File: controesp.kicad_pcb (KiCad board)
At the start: 2 copper layers, 216.9 x 86.5 mm, 73 parts, among them J1 Screw_Terminal_01x08, J13 Conn_01x19_Socket, J14 Conn_01x16_Socket, J15 Screw_Terminal_01x02, J16 Conn_01x19_Socket, J17 Conn_01x19_Socket, J2 Screw_Terminal_01x04, J3 Conn_01x14_Socket, J4 Conn_01x14_Pin, J5 Conn_01x16_Pin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

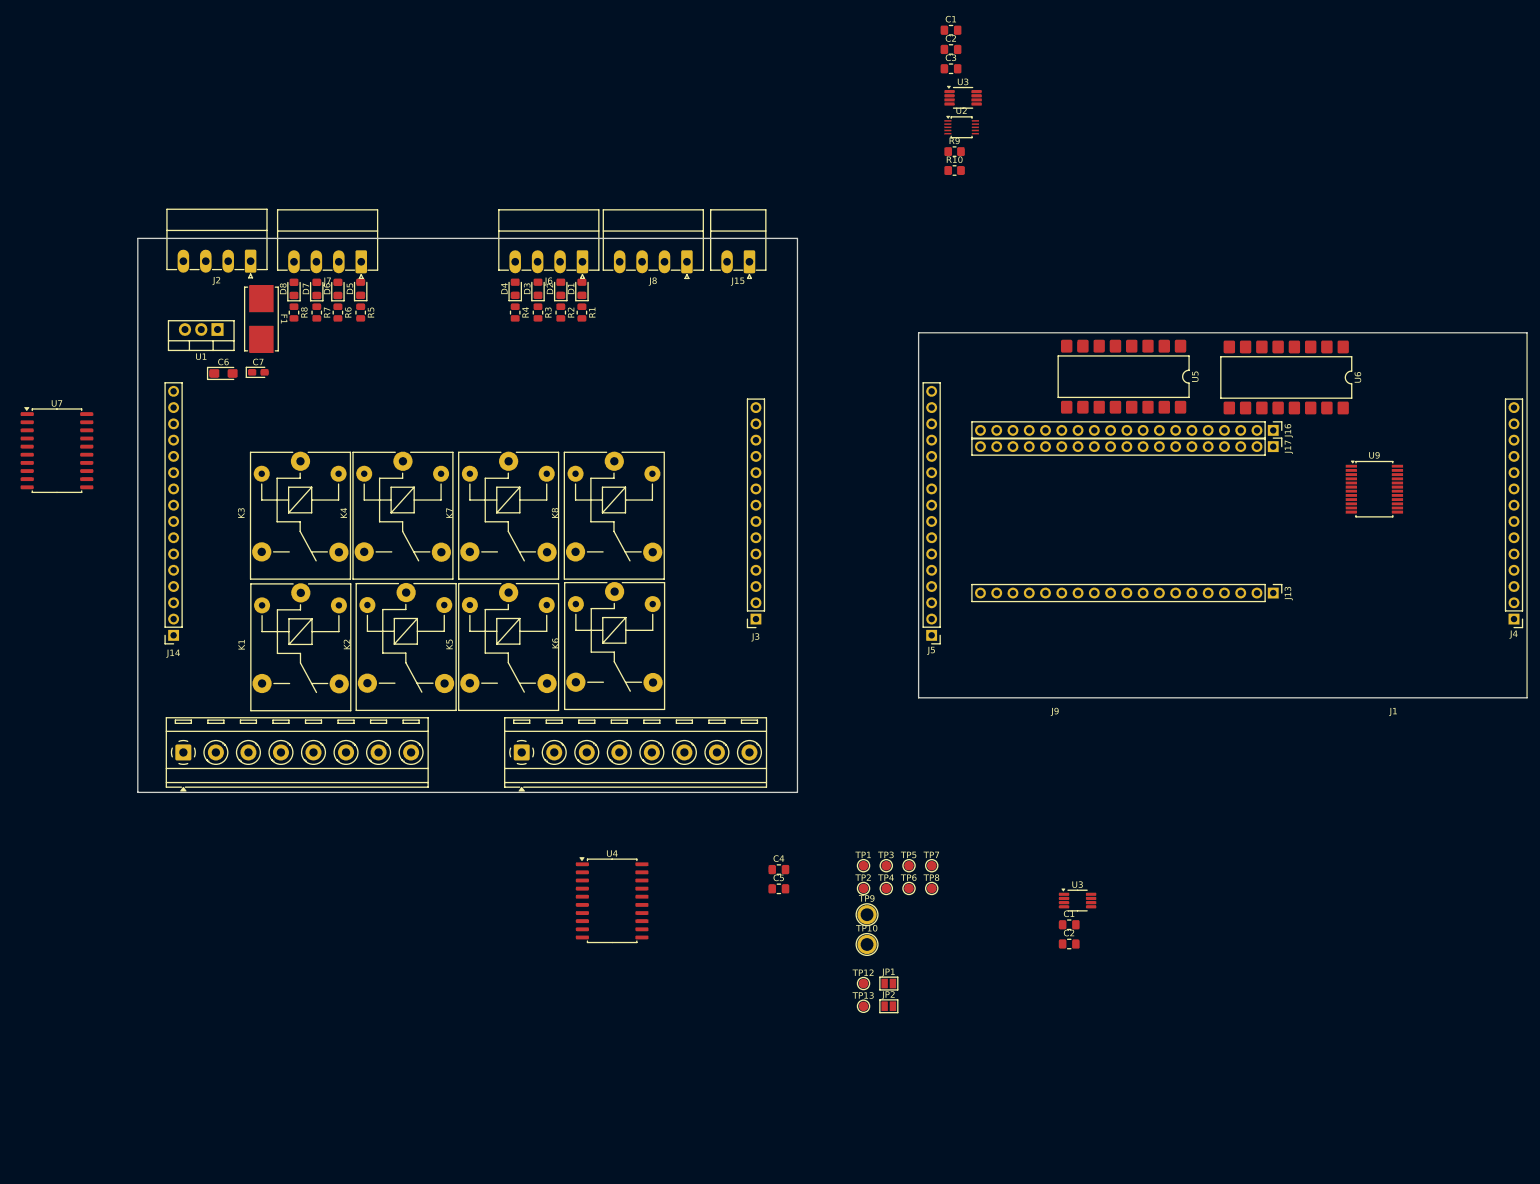
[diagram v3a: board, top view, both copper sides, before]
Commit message: hat routing finished
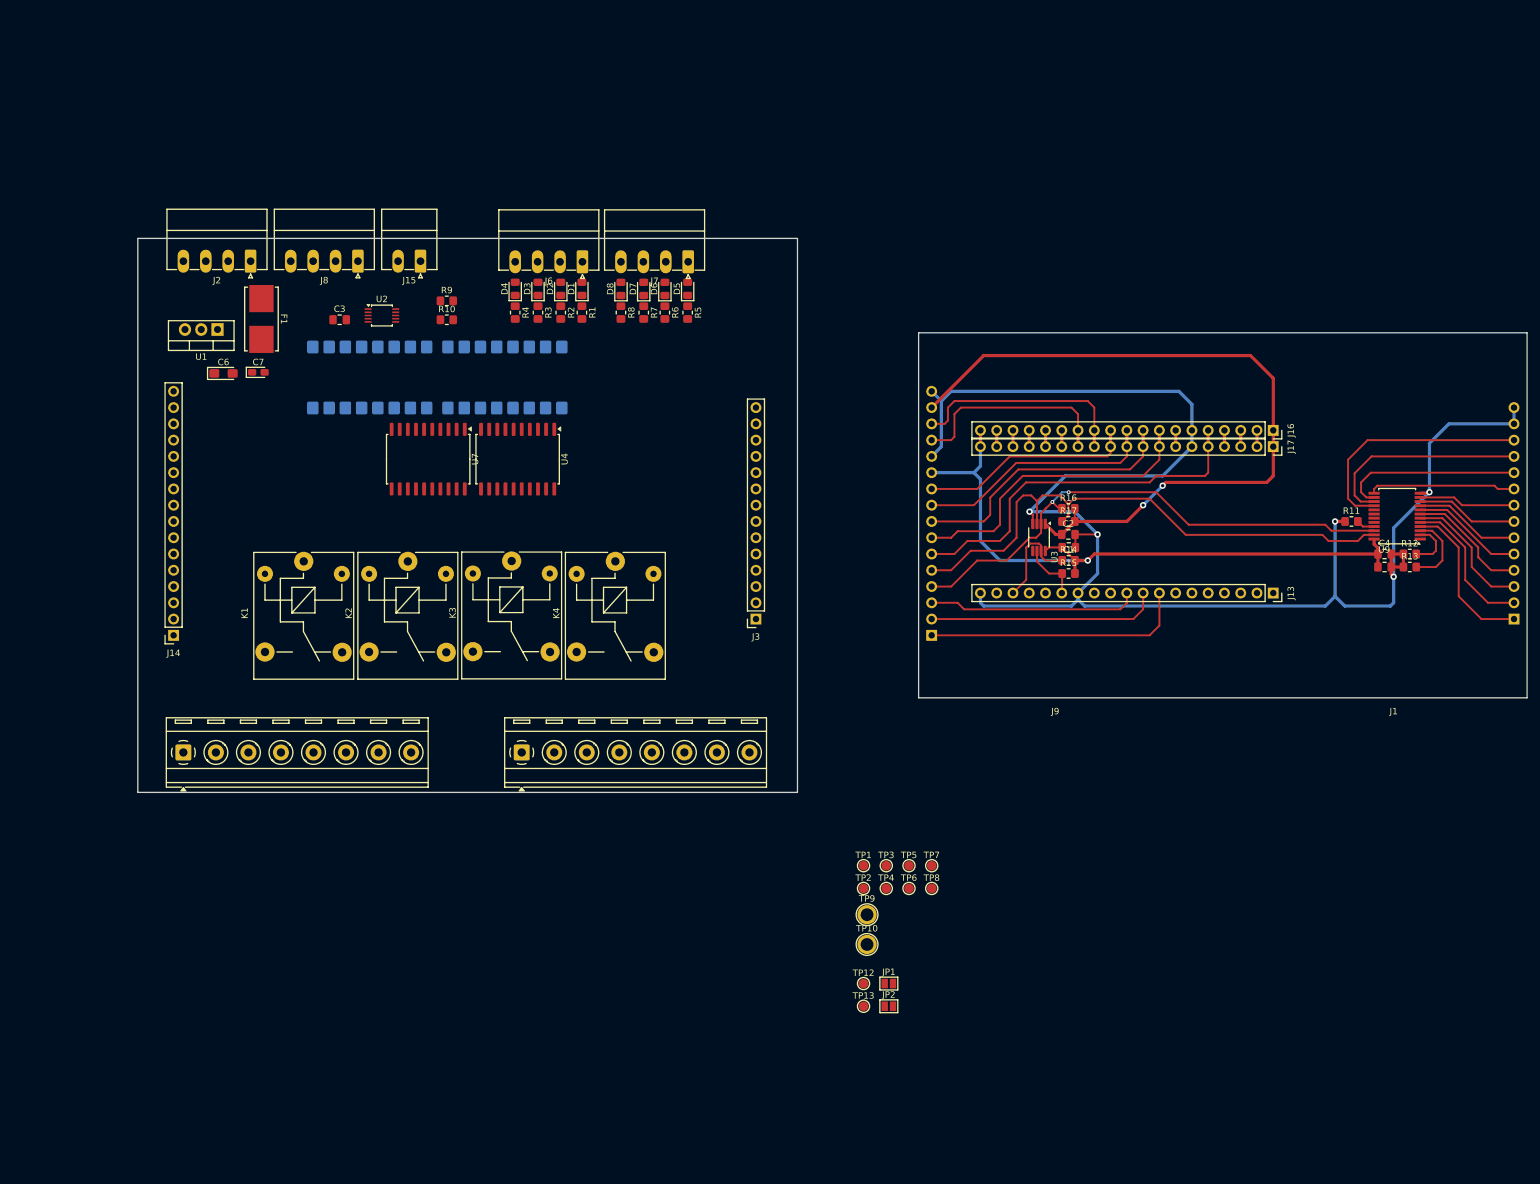
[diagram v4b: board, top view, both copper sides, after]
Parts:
- removed the C1 at (176.8, 17.3)
- removed the C1 at (195.2, 157.0)
- removed the C2 at (176.8, 20.3)
- removed the C2 at (195.2, 160.0)
- removed K5, K6, K7, K8: SANYOU_SRD-S-124D, Relay_THT:Relay_SPDT_SANYOU_SRD_Series_Form_C
- removed the U3 at (196.5, 153.2)
- removed the U3 at (178.6, 27.8)
- added C1: 100nF, Capacitor_SMD:C_0805_2012Metric_Pad1.18x1.45mm_HandSolder, F.Cu at (195.1, 98.0)
- added C2: 100nF, Capacitor_SMD:C_0805_2012Metric_Pad1.18x1.45mm_HandSolder, F.Cu at (195.1, 96.0)
- added R11: 0, Resistor_SMD:R_0805_2012Metric_Pad1.20x1.40mm_HandSolder, F.Cu at (239.3, 94.0)
- added R12: 0, Resistor_SMD:R_0805_2012Metric_Pad1.20x1.40mm_HandSolder, F.Cu at (248.4, 99.1)
- added R13: 0, Resistor_SMD:R_0805_2012Metric_Pad1.20x1.40mm_HandSolder, F.Cu at (248.4, 101.1)
- added R14: 10k, Resistor_SMD:R_0805_2012Metric_Pad1.20x1.40mm_HandSolder, F.Cu at (195.1, 100.1)
- added R15: 10k, Resistor_SMD:R_0805_2012Metric_Pad1.20x1.40mm_HandSolder, F.Cu at (195.1, 102.1)
- added R16: 10k, Resistor_SMD:R_0805_2012Metric_Pad1.20x1.40mm_HandSolder, F.Cu at (195.1, 91.9)
- added R17: 10k, Resistor_SMD:R_0805_2012Metric_Pad1.20x1.40mm_HandSolder, F.Cu at (195.1, 94.0)
- added U3: TCA9517ADGK, Package_SO:VSSOP-8_3x3mm_P0.65mm, F.Cu at (190.5, 96.5)
- J13, J16, J17: footprint Connector_PinHeader_2.54mm:PinHeader_1x19_P2.54mm_Vertical -> Connector_PinSocket_2.54mm:PinSocket_1x19_P2.54mm_Vertical
- J4, J5, U5, U6: moved to B.Cu
- R1, R2, R3, R4, R5, R6, R7, R8: footprint Resistor_SMD:R_0805_2012Metric -> Resistor_SMD:R_0805_2012Metric_Pad1.20x1.40mm_HandSolder
- moved U6 143.1 mm to (86.0, 71.5)
- moved C5 107.1 mm to (244.5, 101.1)
- moved C4 106.6 mm to (244.5, 99.1)
- moved C3 103.2 mm to (81.3, 62.5)
- moved U5 96.6 mm to (107.1, 71.5)
- moved U2 95.2 mm to (87.9, 61.8)
- moved R10 82.6 mm to (98.0, 62.5)
- moved R9 82.6 mm to (98.0, 59.5)
- moved U4 70.5 mm to (109.1, 84.2), turned to -90 degrees
- moved U7 58.0 mm to (95.1, 84.2), turned to -90 degrees
- moved J8 51.4 mm to (84.2, 53.3)
- moved J15 51.4 mm to (93.9, 53.3)
- moved D6 51.1 mm to (132.1, 57.7)
- moved R6 51.1 mm to (132.1, 61.4)
- moved D5 51.1 mm to (135.6, 57.6)
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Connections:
- J14 pad 1: /input/DI1 -> RX2
- J14 pad 10: TX2 -> /input/DI6
- J14 pad 11: RX2 -> +3V3
- J14 pad 13: /input/SCL -> /input/DI7
- J14 pad 14: /input/SDA -> /input/DI8
- J14 pad 2: /input/DI2 -> TX2
- J14 pad 3: /input/DI3 -> /input/SCL
- J14 pad 4: /input/DI4 -> /input/SDA
- J14 pad 5: /input/DI5 -> /input/DI1
- J14 pad 6: /input/DI6 -> /input/DI2
- J14 pad 7: /input/DI7 -> /input/DI3
- J14 pad 8: /input/DI8 -> /input/DI4
- J14 pad 9: +3V3 -> /input/DI5
- J4 pad 13: GND -> /controesp_hat/GND
- J4 pad 14: GND -> /controesp_hat/GND
- J5 pad 1: /controesp_hat/32 -> /controesp_hat/RX2
- J5 pad 10: /controesp_hat/TX2 -> /controesp_hat/25
- J5 pad 11: /controesp_hat/RX2 -> /controesp_hat/3V3
- J5 pad 12: unconnected-(J5-Pin_12-Pad12) -> /controesp_hat/GND
- J5 pad 13: /controesp_hat/SCL_5V -> /controesp_hat/32
- J5 pad 14: /controesp_hat/SDA_5V -> /controesp_hat/33
- J5 pad 2: /controesp_hat/33 -> /controesp_hat/TX2
- J5 pad 3: /controesp_hat/25 -> /controesp_hat/5
- J5 pad 4: /controesp_hat/26 -> /controesp_hat/SCL_5V
- J5 pad 5: /controesp_hat/27 -> /controesp_hat/SDA_5V
- J5 pad 6: /controesp_hat/14 -> /controesp_hat/13
- J5 pad 7: /controesp_hat/5 -> /controesp_hat/14
- J5 pad 8: /controesp_hat/13 -> /controesp_hat/27
- J5 pad 9: /controesp_hat/3V3 -> /controesp_hat/26
- J9 pad 1: COM2 -> GND
- U4 pad 11: Net-(U4-O8) -> Net-(J9-Pin_5)
- U4 pad 12: Net-(U4-O7) -> Net-(J9-Pin_4)
- U4 pad 13: Net-(U4-O6) -> Net-(J9-Pin_3)
- U4 pad 14: Net-(U4-O5) -> Net-(J9-Pin_2)
- U9 pad 2: /controesp_hat/GND -> Net-(U9-A1)
- U9 pad 21: /controesp_hat/GND -> Net-(U9-A0)
- U9 pad 3: /controesp_hat/GND -> Net-(U9-A2)
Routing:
- net /controesp_hat/GND: track 0.00 -> 256.6 mm, vias 0 -> 5
- net /controesp_hat/VCC: track 0.00 -> 115.5 mm, vias 0 -> 2
- net /controesp_hat/3V3: track 0.00 -> 102.8 mm, vias 0 -> 1
- net /controesp_hat/SDA_5V: track 0.00 -> 88.7 mm
- net /controesp_hat/SCL_5V: track 0.00 -> 81.4 mm, vias 0 -> 2
- net /controesp_hat/13: track 0.00 -> 58.0 mm
- net /controesp_hat/14: track 0.00 -> 47.6 mm
- net /controesp_hat/27: track 0.00 -> 42.9 mm
- net /controesp_hat/RX2: track 0.00 -> 41.3 mm
- net /controesp_hat/P13: track 0.00 -> 37.8 mm
- net /controesp_hat/26: track 0.00 -> 37.7 mm
- net /controesp_hat/TX2: track 0.00 -> 36.2 mm
- net /controesp_hat/33: track 0.00 -> 34.6 mm
- net /controesp_hat/25: track 0.00 -> 33.8 mm
- net /controesp_hat/P12: track 0.00 -> 32.9 mm
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
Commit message: started base layout
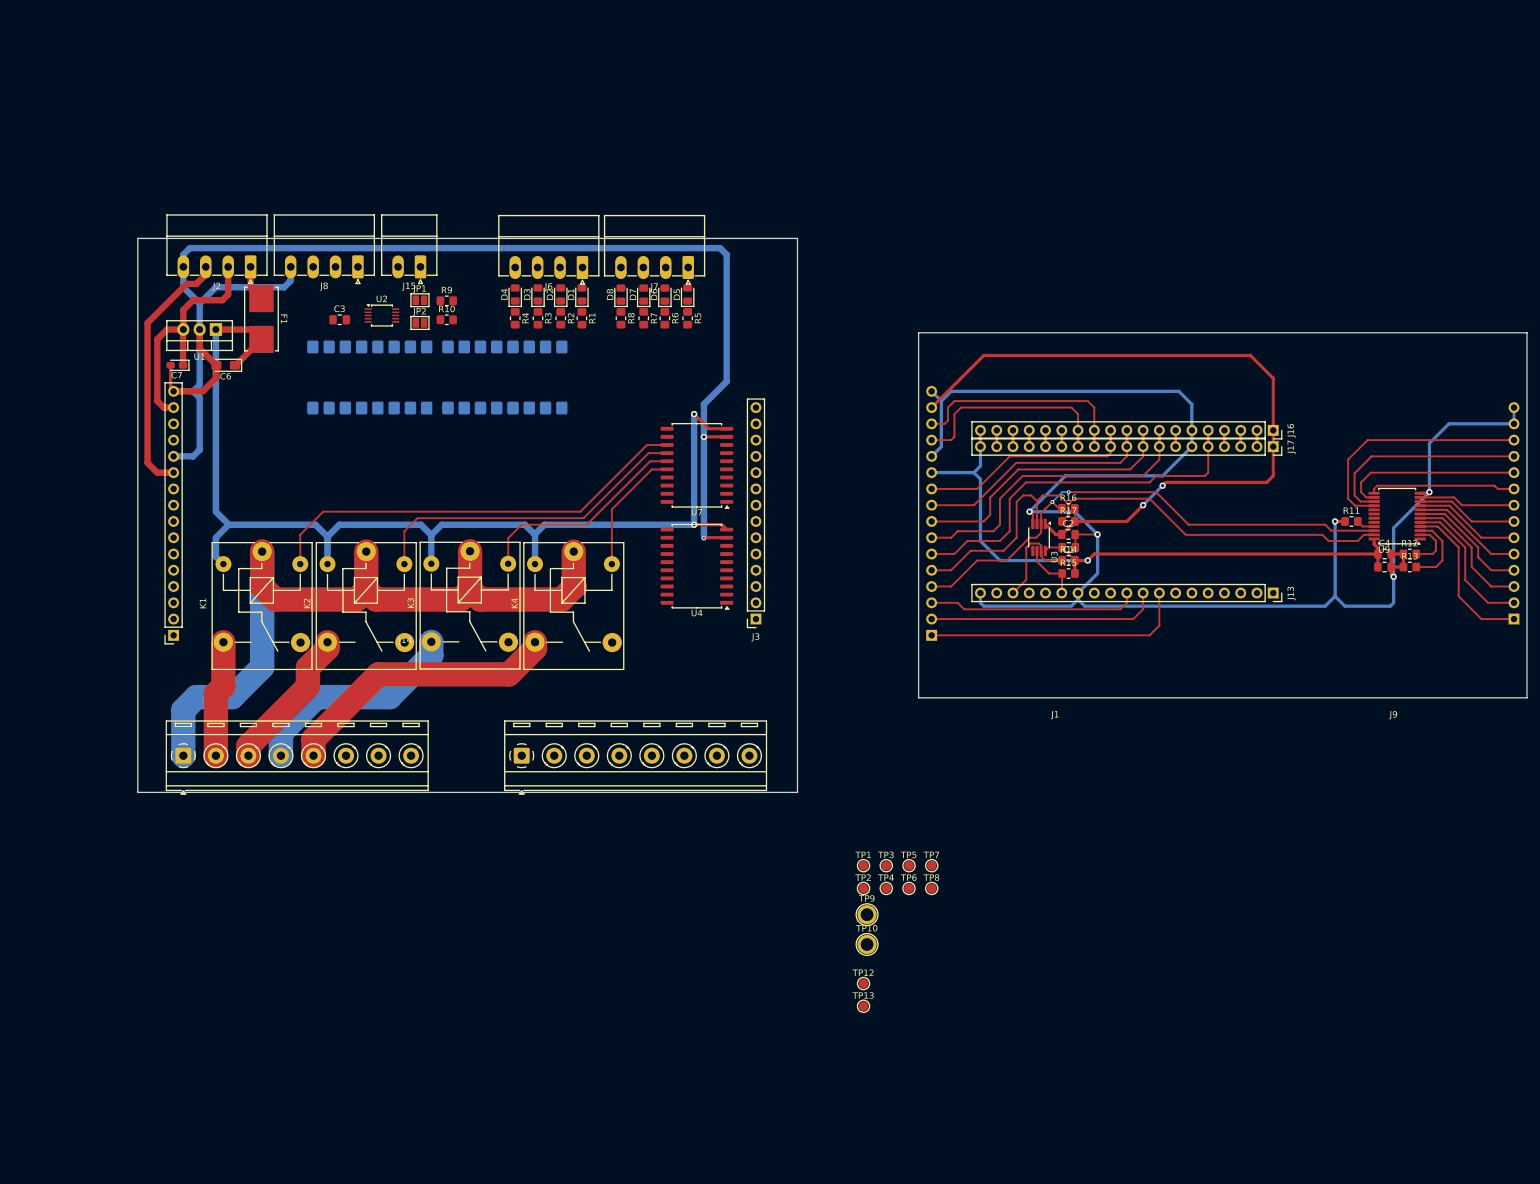
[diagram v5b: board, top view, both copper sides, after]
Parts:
- moved JP2 129.4 mm to (93.8, 63.0)
- moved JP1 129.4 mm to (93.8, 59.4)
- moved J1 52.8 mm to (56.9, 130.6)
- moved J9 52.8 mm to (109.7, 130.6)
- moved U7 42.0 mm to (137.1, 85.2), turned to 180 degrees
- moved U4 32.6 mm to (137.1, 101.0), turned to 180 degrees
- moved C7 12.8 mm to (55.9, 69.6), turned to 180 degrees
- moved K1 6.67 mm to (69.2, 98.7)
- moved K2 6.67 mm to (85.5, 98.7)
- moved K3 6.67 mm to (101.7, 98.6)
- moved K4 6.67 mm to (117.9, 98.7)
- moved C6 1.31 mm to (63.5, 69.6), turned to 180 degrees
- moved D1 0.89 mm to (119.1, 58.5)
- moved D2 0.89 mm to (115.8, 58.5)
- moved D3 0.89 mm to (112.3, 58.5)
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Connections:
- J3 pad 10: /powerOutput/DO10 -> DO10
- J3 pad 11: /powerOutput/DO11 -> DO11
- J3 pad 12: /powerOutput/DO12 -> DO12
- J3 pad 9: /powerOutput/DO9 -> DO9
- J9 pad 2: Net-(J9-Pin_2) -> unconnected-(J9-Pin_2-Pad2)
- J9 pad 3: Net-(J9-Pin_3) -> unconnected-(J9-Pin_3-Pad3)
- J9 pad 4: Net-(J9-Pin_4) -> unconnected-(J9-Pin_4-Pad4)
- J9 pad 5: Net-(J9-Pin_5) -> DO9
- K1 pad 5: Net-(U4-O1) -> DO14
- K2 pad 5: Net-(U4-O2) -> DO13
- K3 pad 5: Net-(U4-O3) -> DO12
- K4 pad 5: Net-(U4-O4) -> DO11
- TP1 pad 1: Net-(U4-O1) -> DO14
- TP2 pad 1: Net-(U4-O2) -> DO13
- TP3 pad 1: Net-(U4-O3) -> DO12
- TP4 pad 1: Net-(U4-O4) -> DO11
- U4 pad 11: Net-(J9-Pin_5) -> unconnected-(U4-O8-Pad11)
- U4 pad 12: Net-(J9-Pin_4) -> unconnected-(U4-O7-Pad12)
- U4 pad 13: Net-(J9-Pin_3) -> unconnected-(U4-O6-Pad13)
- U4 pad 14: Net-(J9-Pin_2) -> unconnected-(U4-O5-Pad14)
- U4 pad 15: Net-(U4-O4) -> unconnected-(U4-O4-Pad15)
- U4 pad 16: Net-(U4-O3) -> unconnected-(U4-O3-Pad16)
- U4 pad 17: Net-(U4-O2) -> unconnected-(U4-O2-Pad17)
- U4 pad 18: Net-(U4-O1) -> unconnected-(U4-O1-Pad18)
- U7 pad 1: /powerOutput/DO9 -> DO9
- U7 pad 13: DO6 -> DO14
- U7 pad 14: DO5 -> DO13
- U7 pad 15: DO4 -> DO12
- U7 pad 16: DO3 -> DO11
- U7 pad 17: DO2 -> DO10
- U7 pad 18: DO1 -> DO9
- U7 pad 2: /powerOutput/DO10 -> DO10
- U7 pad 3: /powerOutput/DO11 -> DO11
- U7 pad 4: /powerOutput/DO12 -> DO12
- U7 pad 5: unconnected-(U7-I5-Pad5) -> DO13
- U7 pad 6: unconnected-(U7-I6-Pad6) -> DO14
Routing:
- net GND: track 0.00 -> 216.7 mm, vias 0 -> 2
- net +24V: track 0.00 -> 171.3 mm, vias 0 -> 2
- net COM1: track 0.00 -> 116.2 mm
- net DO14: track 0.00 -> 67.7 mm
- net DO13: track 0.00 -> 51.2 mm
- net Net-(J1-Pin_5): track 0.00 -> 44.0 mm
- net +3V3: track 0.00 -> 40.0 mm
- net +5V: track 0.00 -> 38.3 mm
- net Net-(J1-Pin_4): track 0.00 -> 34.2 mm
- net DO12: track 0.00 -> 33.8 mm
- net Net-(J1-Pin_3): track 0.00 -> 22.8 mm
- net DO11: track 0.00 -> 19.8 mm
- net Net-(J1-Pin_2): track 0.00 -> 18.2 mm
- net Net-(J2-Pin_1): track 0.00 -> 5.65 mm

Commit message: von ben
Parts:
- removed TP12: SDA, TestPoint:TestPoint_Pad_D1.5mm
- removed TP13: SCL, TestPoint:TestPoint_Pad_D1.5mm
- U5, U6: moved to F.Cu
- moved TP1 102.4 mm to (75.2, 95.2)
- moved TP2 91.0 mm to (91.4, 95.2)
- moved TP3 78.9 mm to (107.7, 95.2)
- moved TP4 70.6 mm to (123.7, 95.2)
- moved U6 29.2 mm to (113.3, 81.8)
- moved U5 18.1 mm to (92.2, 81.8)
- moved R10 10.7 mm to (87.9, 59.2), turned to -90 degrees
- moved C3 8.26 mm to (83.8, 70.4), turned to 180 degrees
- moved JP2 5.20 mm to (90.4, 59.1), turned to -90 degrees
- moved U2 4.91 mm to (85.6, 66.2), turned to -90 degrees
- moved R9 4.57 mm to (93.5, 59.2), turned to -90 degrees
- moved JP1 2.71 mm to (96.5, 59.1), turned to -90 degrees
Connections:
- J14 pad 1: RX2 -> /input/DI1
- J14 pad 10: /input/DI6 -> /input/SCL
- J14 pad 13: /input/DI7 -> RX2
- J14 pad 14: /input/DI8 -> TX2
- J14 pad 2: TX2 -> /input/DI2
- J14 pad 3: /input/SCL -> /input/DI8
- J14 pad 4: /input/SDA -> /input/DI7
- J14 pad 5: /input/DI1 -> /input/DI3
- J14 pad 6: /input/DI2 -> /input/DI4
- J14 pad 7: /input/DI3 -> /input/DI5
- J14 pad 8: /input/DI4 -> /input/DI6
- J14 pad 9: /input/DI5 -> /input/SDA
- J3 pad 10: DO10 -> /powerOutput/DO10
- J3 pad 11: DO11 -> /powerOutput/DO11
- J3 pad 12: DO12 -> /powerOutput/DO12
- J5 pad 1: /controesp_hat/RX2 -> /controesp_hat/32
- J5 pad 10: /controesp_hat/25 -> /controesp_hat/SCL_5V
- J5 pad 13: /controesp_hat/32 -> /controesp_hat/RX2
- J5 pad 14: /controesp_hat/33 -> /controesp_hat/TX2
- J5 pad 2: /controesp_hat/TX2 -> /controesp_hat/33
- J5 pad 4: /controesp_hat/SCL_5V -> unconnected-(J5-Pin_4-Pad4)
- J5 pad 5: /controesp_hat/SDA_5V -> unconnected-(J5-Pin_5-Pad5)
- J5 pad 9: /controesp_hat/26 -> /controesp_hat/SDA_5V
- J8 pad 2: TX2 -> RX2
- J8 pad 3: RX2 -> TX2
- JP1 pad 1: Net-(JP1-A) -> Net-(J15-Pin_1)
- JP2 pad 1: Net-(JP2-A) -> Net-(J15-Pin_2)
- K1 pad 5: DO14 -> DO.14
- K2 pad 5: DO13 -> DO.13
- K3 pad 5: DO12 -> DO.12
- K4 pad 5: DO11 -> DO.11
- R10 pad 2: Net-(JP2-A) -> Net-(U2-AIN1)
- R9 pad 2: Net-(JP1-A) -> Net-(U2-AIN0)
- TP1 pad 1: DO14 -> DO.14
- TP2 pad 1: DO13 -> DO.13
- TP3 pad 1: DO12 -> DO.12
- TP4 pad 1: DO11 -> DO.11
- U2 pad 4: Net-(JP1-A) -> Net-(U2-AIN0)
- U2 pad 5: Net-(JP2-A) -> Net-(U2-AIN1)
- U7 pad 13: DO14 -> DO.14
- U7 pad 14: DO13 -> DO.13
- U7 pad 15: DO12 -> DO.12
- U7 pad 16: DO11 -> DO.11
- U7 pad 17: DO10 -> DO.10
- U7 pad 18: DO9 -> DO.9
- U7 pad 2: DO10 -> /powerOutput/DO10
- U7 pad 3: DO11 -> /powerOutput/DO11
- U7 pad 4: DO12 -> /powerOutput/DO12
- U7 pad 5: DO13 -> /powerOutput/DO13
- U7 pad 6: DO14 -> /powerOutput/DO14
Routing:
- net DO.14: track 0.00 -> 68.1 mm
- net DO14: track 67.7 -> 0.00 mm
- net +5V: track 38.3 -> 101.6 mm, vias 0 -> 2
- net /input/SCL: track 0.00 -> 59.1 mm
- net /input/SDA: track 0.00 -> 58.2 mm
- net DO.13: track 0.00 -> 51.3 mm
- net DO13: track 51.2 -> 0.00 mm
- net RX2: track 0.00 -> 42.0 mm
- net TX2: track 0.00 -> 37.6 mm
- net DO.12: track 0.00 -> 34.5 mm
- net GND: track 216.7 -> 251.0 mm, vias 2 -> 4
- net DO12: track 33.8 -> 0.00 mm
- net /controesp_hat/33: track 34.6 -> 2.54 mm
- net /controesp_hat/TX2: track 36.2 -> 67.5 mm, vias 0 -> 2
- net /controesp_hat/32: track 32.5 -> 2.54 mm
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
